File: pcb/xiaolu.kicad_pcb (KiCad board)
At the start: 2 copper layers, 51 x 76 mm, 39 parts, among them J1 Conn_01x04_Male, J2 TRRS, SW1 SW_Push, SW10 SW_Push, SW11 SW_Push, SW12 SW_Push, SW13 SW_Push, SW14 SW_Push, SW15 SW_Push, SW16 SW_Push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

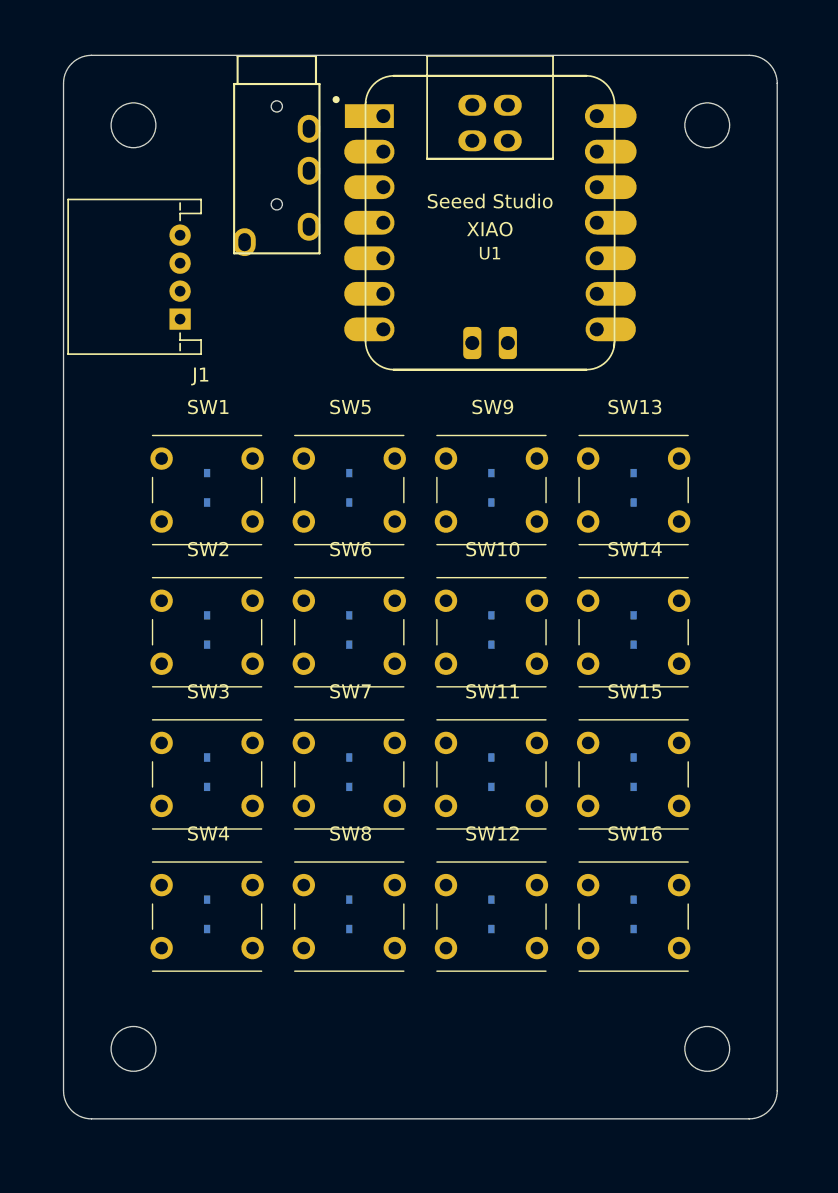
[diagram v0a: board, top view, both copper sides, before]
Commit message: replace XIAO footprint with XIAO-Generic-Hybrid-14P-2.54-21X17.8MM
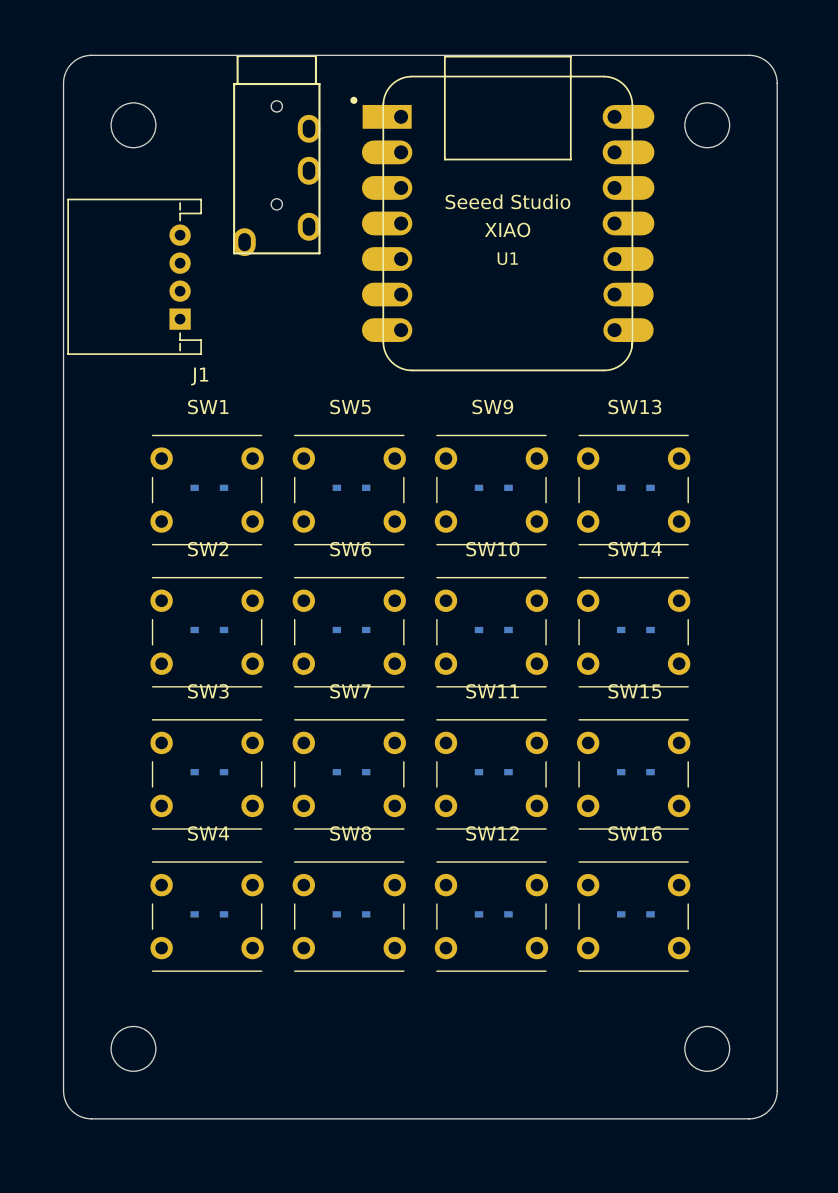
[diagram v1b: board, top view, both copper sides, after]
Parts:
- U1: footprint Xiaolu-Specific:XIAO-SAMD21-RP2040-Hybrid-14P-2.54-21X17.8MM -> Xiaolu-Specific:XIAO-Generic-Hybrid-14P-2.54-21X17.8MM
- moved D13 30.6 mm to (91.7, 81.1), turned to 180 degrees
- moved D1 30.5 mm to (61.2, 81.1), turned to 180 degrees
- moved D16 30.5 mm to (91.7, 111.6), turned to 180 degrees
- moved D4 30.3 mm to (61.2, 111.6), turned to 180 degrees
- moved D14 22.9 mm to (91.7, 91.3), turned to 180 degrees
- moved D9 22.9 mm to (81.5, 81.1), turned to 180 degrees
- moved D15 22.8 mm to (91.7, 101.4), turned to 180 degrees
- moved D5 22.8 mm to (71.4, 81.1), turned to 180 degrees
- moved D12 22.6 mm to (81.5, 111.6), turned to 180 degrees
- moved D2 22.6 mm to (61.2, 91.3), turned to 180 degrees
- moved D8 22.6 mm to (71.4, 111.6), turned to 180 degrees
- moved D3 22.6 mm to (61.2, 101.4), turned to 180 degrees
- moved D10 10.3 mm to (81.5, 91.3), turned to 180 degrees
- moved D11 10.2 mm to (81.5, 101.4), turned to 180 degrees
- moved D6 10.2 mm to (71.4, 91.3), turned to 180 degrees
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
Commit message: wiring
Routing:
- net row3: track 0.00 -> 96.4 mm
- net row2: track 0.00 -> 96.2 mm
- net col0: track 0.00 -> 92.4 mm
- net row1: track 0.00 -> 89.2 mm
- net col1: track 0.00 -> 81.7 mm
- net col2: track 0.00 -> 74.9 mm
- net col3: track 0.00 -> 67.8 mm
- net row0: track 0.00 -> 66.2 mm
- net GND: track 0.00 -> 45.3 mm
- net +5V: track 0.00 -> 41.6 mm
- net SDA: track 0.00 -> 28.3 mm
- net SCL: track 0.00 -> 25.5 mm
- net Net-(D14-Pad2): track 0.00 -> 13.9 mm
- net Net-(D8-Pad2): track 0.00 -> 8.64 mm
- net Net-(D4-Pad2): track 0.00 -> 8.64 mm
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- added copper zone on B.Cu, net GND
- added copper zone on F.Cu, net GND

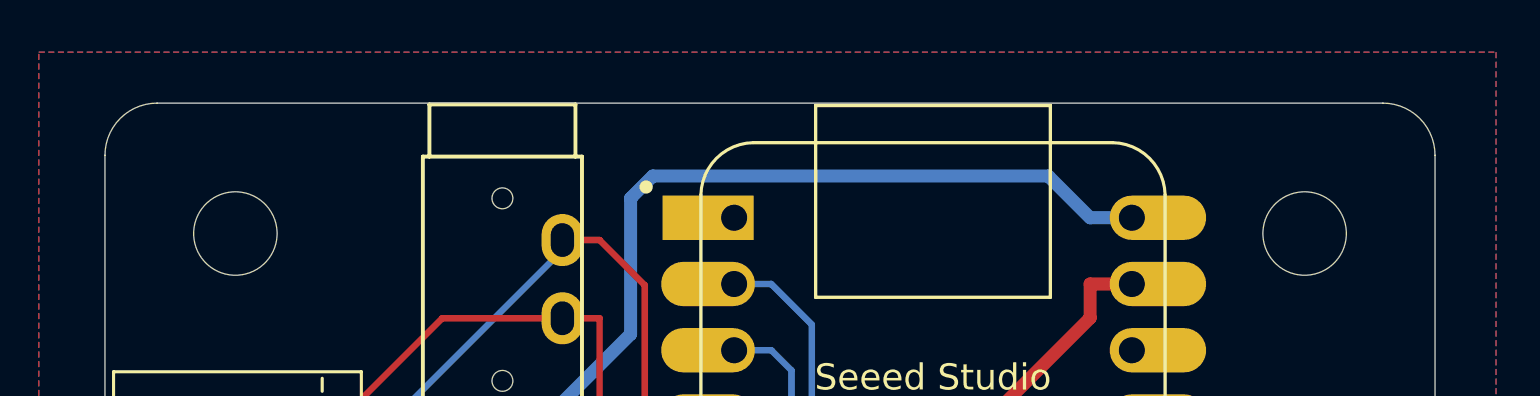
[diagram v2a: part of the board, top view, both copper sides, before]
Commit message: add notch for XIAO-usb and TRRS-jack to the PCB board edge
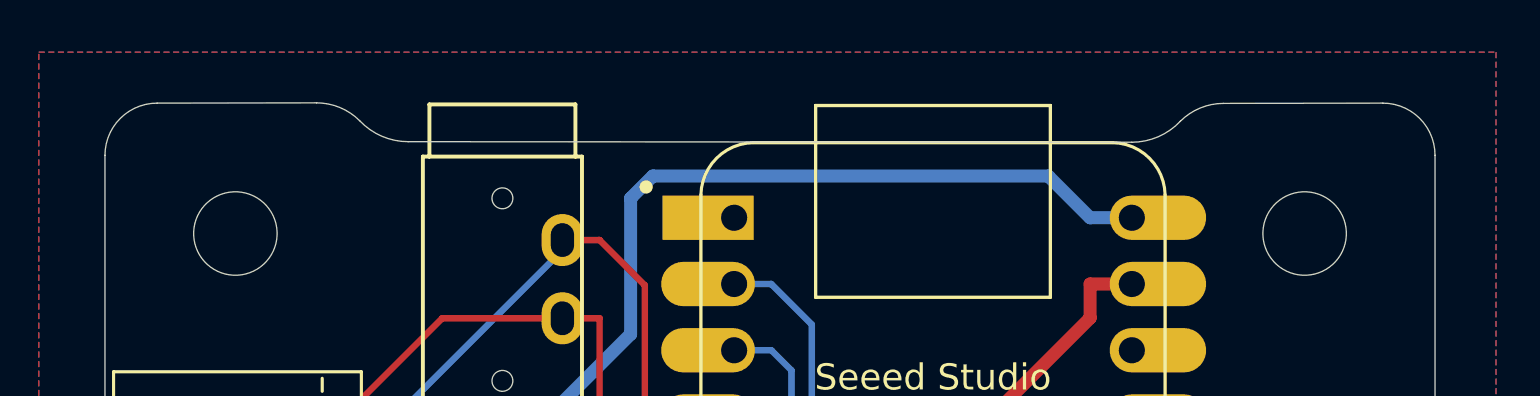
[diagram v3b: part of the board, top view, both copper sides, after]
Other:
- outline, holes or cut-outs redrawn
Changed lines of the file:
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@@
     )
   )
-  (gr_line (start 99.8 50.214214) (end 52.8 50.214214) (layer "Edge.Cuts") (width 0.05))
+  (gr_arc (start 62.43 51.693144) (mid 61.415537 51.483621) (end 60.567088 50.889339) (layer "Edge.Cuts") (width 0.05))
+  (gr_line (start 99.8 50.214214) (end 93.688242 50.224749) (layer "Edge.Cuts") (width 0.05))
   (gr_line (start 101.8 52.214214) (end 101.8 124.214214) (layer "Edge.Cuts") (width 0.05))
   (gr_arc (start 99.8 50.214214) (mid 101.214214 50.8) (end 101.8 52.214214) (layer "Edge.Cuts") (width 0.05))
   (gr_arc (start 52.8 126.214214) (mid 51.385786 125.628428) (end 50.8 124.214214) (layer "Edge.Cuts") (width 0.05))
+  (gr_arc (start 92.032912 50.910409) (mid 92.792384 50.402946) (end 93.688242 50.224749) (layer "Edge.Cuts") (width 0.05))
   (gr_arc (start 50.8 52.214214) (mid 51.385786 50.8) (end 52.8 50.214214) (layer "Edge.Cuts") (width 0.05))
   (gr_arc (start 101.8 124.214214) (mid 101.214214 125.628428) (end 99.8 126.214214) (layer "Edge.Cuts") (width 0.05))
   (gr_line (start 99.8 126.214214) (end 52.8 126.214214) (layer "Edge.Cuts") (width 0.05))
+  (gr_arc (start 92.032912 50.910409) (mid 91.184463 51.504691) (end 90.17 51.714214) (layer "Edge.Cuts") (width 0.05))
+  (gr_arc (start 58.911758 50.203679) (mid 59.807616 50.381876) (end 60.567088 50.889339) (layer "Edge.Cuts") (width 0.05))
   (gr_line (start 50.8 52.214214) (end 50.8 124.214214) (layer "Edge.Cuts") (width 0.05))
+  (gr_line (start 90.17 51.714214) (end 62.43 51.693144) (layer "Edge.Cuts") (width 0.05))
+  (gr_line (start 58.911758 50.203679) (end 52.8 50.214214) (layer "Edge.Cuts") (width 0.05))
   (dimension (type aligned) (layer "Eco1.User")
     (pts (xy 56.06 116.76) (xy 96.54 116.76))
